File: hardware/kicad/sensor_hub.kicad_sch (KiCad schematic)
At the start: 63 parts, among them J1 1-1478035-0, J10 Wago-Relay2, J11 Spare-GPIO, J2 Wago-DS18B20, J3 Wago-DHT22, J4 Wago-PIR, J5 Wago-GP16, J6 Wago-GP17, J7 Wago-Relay1, J8 Phoenix-EC4pin, J9 Phoenix-Power, K1 G2RL-1-E DC5, K2 G2RL-1-E DC5, Q1 BC817-40, Q2 BSS84PXUMA1, Q3 BC817-40, U1 Pico WH, U2 ADS1115IDGSR, U3 LMP91200SD/NOPB, U4 AD8603ARTZ-R2, U5 AP2112K-3.3TRG1, U6 VEML7700-TT

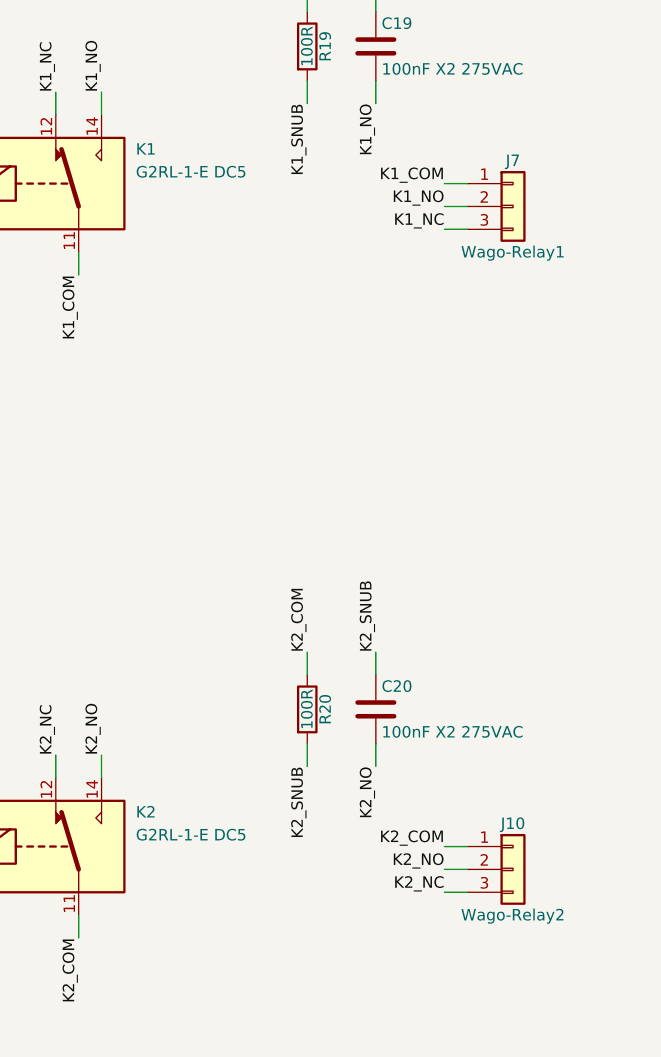
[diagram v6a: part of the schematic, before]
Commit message: hardware: upright relays with terminals aligned to contact rows, remap W6/W7 pins
Co-Authored-By: Claude Opus 5.5 <noreply@anthropic.com>
Claude-Session: https://claude.ai/code/session_01PDHupfXBxwLmo1MxXKJEdB
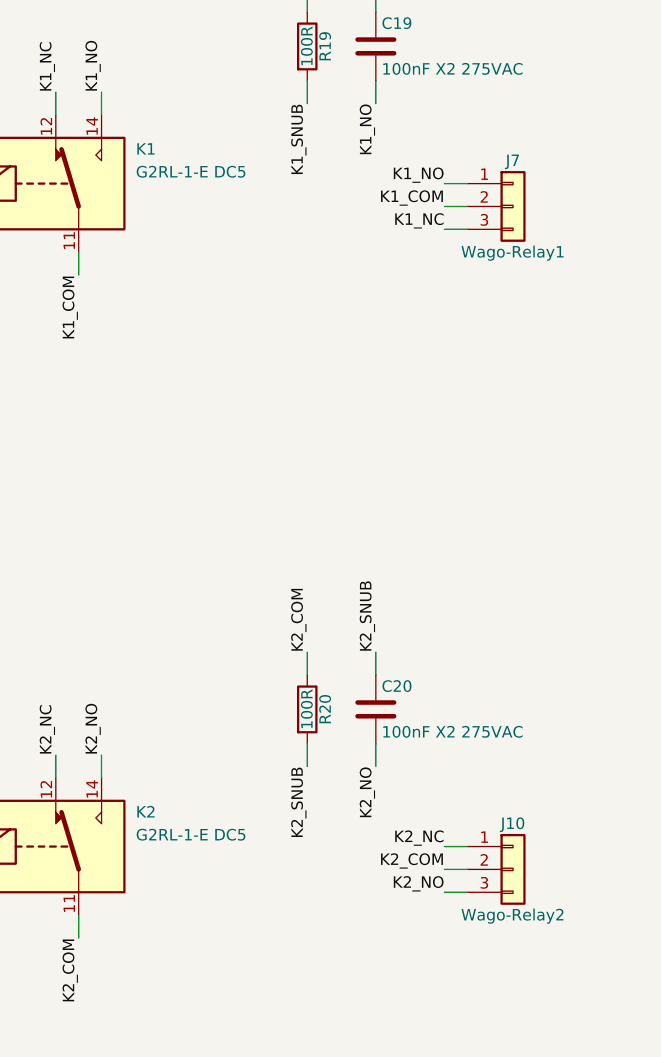
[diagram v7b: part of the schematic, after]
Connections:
- net K1_COM: now also J7.2 (Pin_2); no longer J7.1 (Pin_1)
- net K1_NO: now also J7.1 (Pin_1); no longer J7.2 (Pin_2)
- net K2_COM: now also J10.2 (Pin_2); no longer J10.1 (Pin_1)
- net K2_NC: now also J10.1 (Pin_1); no longer J10.3 (Pin_3)
- net K2_NO: now also J10.3 (Pin_3); no longer J10.2 (Pin_2)

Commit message: hardware: Wago push-in for J8/J9, exposed pH guard, JLCPCB SMD assembly files
- J8 (EC) / J9 (5V in): Phoenix screw -> Wago 2601-1104 / 2601-1102, same
  family as J2-J6; power block moved down 3.5 mm, J2-J6 row shifted 0.6 mm
- pH guard: top-side guard copper exposed (mask opening = fill - 0.1 mm,
  footprint silkscreen kept masked); CLAUDE.md analog-zone rules updated
- route_pcb finish rerunnable (clears its own pours)
- jlc_export.py + fab/: gerbers.zip, bom_jlc.csv, cpl_jlc.csv (39 SMD parts,
  17 LCSC lines, DNP and THT excluded); bom.csv gains an lcsc column
- U4 order code fixed: AD8603AUJZ (ARTZ does not exist)

Co-Authored-By: Claude Opus 5.5 <noreply@anthropic.com>
Claude-Session: https://claude.ai/code/session_01PDHupfXBxwLmo1MxXKJEdB
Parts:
- J8: value Phoenix-EC4pin -> Wago-EC4pin; footprint TerminalBlock_Phoenix:TerminalBlock_Phoenix_PT-1,5-4-3.5-H_1x04_P3.50mm_Horizontal -> TerminalBlock_WAGO:TerminalBlock_WAGO_2601-1104_1x04_P3.50mm_Horizontal
- J9: value Phoenix-Power -> Wago-Power; footprint TerminalBlock_Phoenix:TerminalBlock_Phoenix_PT-1,5-2-5.0-H_1x02_P5.00mm_Horizontal -> TerminalBlock_WAGO:TerminalBlock_WAGO_2601-1102_1x02_P3.50mm_Horizontal
- U4: value AD8603ARTZ-R2 -> AD8603AUJZ
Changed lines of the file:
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@@
 			)
 		)
-		(property "Value" "Phoenix-EC4pin"
+		(property "Value" "Wago-EC4pin"
 			(at 35.56 182.88 0)
 			(show_name no)
@@
 			)
 		)
-		(property "Footprint" "TerminalBlock_Phoenix:TerminalBlock_Phoenix_PT-1,5-4-3.5-H_1x04_P3.50mm_Horizontal"
+		(property "Footprint" "TerminalBlock_WAGO:TerminalBlock_WAGO_2601-1104_1x04_P3.50mm_Horizontal"
 			(at 35.56 175.26 0)
 			(hide yes)
@@
 			)
 		)
-		(property "Value" "AD8603ARTZ-R2"
+		(property "Value" "AD8603AUJZ"
 			(at 109.22 93.98 0)
 			(show_name no)
@@
 			)
 		)
-		(property "Value" "Phoenix-Power"
+		(property "Value" "Wago-Power"
 			(at 35.56 50.8 0)
 			(show_name no)
@@
 			)
 		)
-		(property "Footprint" "TerminalBlock_Phoenix:TerminalBlock_Phoenix_PT-1,5-2-5.0-H_1x02_P5.00mm_Horizontal"
+		(property "Footprint" "TerminalBlock_WAGO:TerminalBlock_WAGO_2601-1102_1x02_P3.50mm_Horizontal"
 			(at 35.56 45.72 0)
 			(hide yes)
